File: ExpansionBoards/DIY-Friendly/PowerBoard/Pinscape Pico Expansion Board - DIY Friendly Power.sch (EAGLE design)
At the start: 83 parts, among them IC1 UCC27524P, IC10 ULN2803A, IC11 ULN2803A, IC12 ULN2803A, IC13 DS1307+, IC2 UCC27524P, IC3 UCC27524P, IC4 UCC27524P, IC5 UCC27524P, IC6 UCC27524P, IC7 UCC27524P, IC8 UCC27524P, IC9 ULN2803A, J1 640445-9, J2 640445-9, J3 640445-6, J4 1-640456-0, J5 1-640456-0, J6 1-640456-0, J7 1-640456-0, Q1 STP19NF20, Q10 STP19NF20, Q11 STP19NF20, Q12 STP19NF20, Q13 STP19NF20, Q14 STP19NF20, Q15 STP19NF20, Q16 STP19NF20, Q17 2N2222A, Q18 2N2222A, Q2 STP19NF20, Q3 STP19NF20, Q4 STP19NF20, Q5 STP19NF20, Q6 STP19NF20, Q7 STP19NF20, Q8 STP19NF20, Q9 STP19NF20, Y1 ECS-.327-12.5-13X-C

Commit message: Exp boards: update gate resistors in BOMs
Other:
- note added: "Note: Gate resistor value of 200 Ohms is chosen to protect UCC27524P against damage due to excessive power dissipation during PWM switching. In principle, the gate resistor is primarily to suppress ringing, which only requires a small resistor in the 5 to 10 Ohm range. But practical testing suggests that UCC27524P may be vulnerable to overload when used with MOSFETs with high input capacitance (C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"
- note removed: "Note: Gate resistor value of 200 Ohms is chosen to protect UCC27524P against damage due to excessive power dissipation during PWM switching. In principle, the gate resistor is primarily to suppress ringing, which only requires a small resistor in the 5 to 10 Ohm range. But practical testing shows that UCC27524P is vulnerable to overload when used with MOSFETs with high input capacitance (C[ISS]).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"
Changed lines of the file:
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@@
 In principle, the gate resistor is primarily to suppress
 ringing, which only requires a small resistor in the 5
-to 10 Ohm range.  But practical testing shows that
-UCC27524P is vulnerable to overload when used
+to 10 Ohm range.  But practical testing suggests that
+UCC27524P may be vulnerable to overload when used
 with MOSFETs with high input capacitance (C[ISS]).
 200 Ohms appears safe for common FETs such as

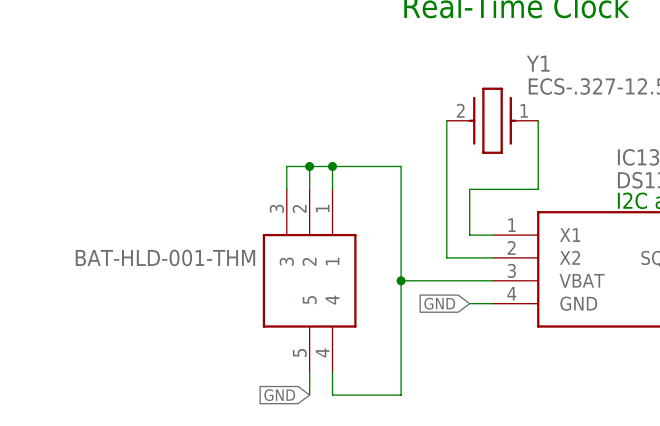
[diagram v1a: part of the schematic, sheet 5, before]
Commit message: exp board: DIY power: change battery holder to snap-in type
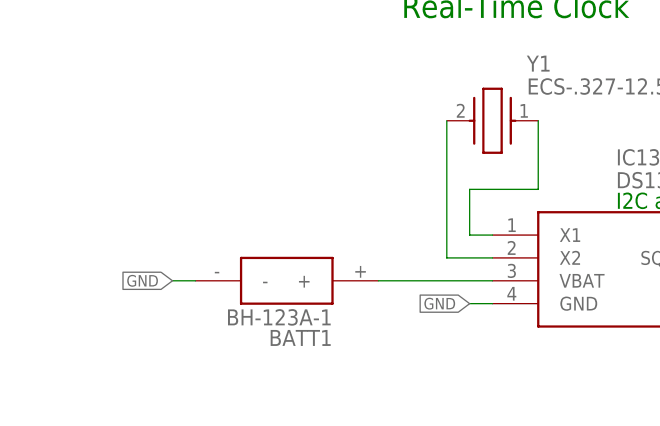
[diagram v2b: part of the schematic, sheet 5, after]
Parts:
- BATT1: value BAT-HLD-001-THM -> BH-123A-1; device SamacSys_Parts:BAT-HLD-001-THM -> SamacSys_Parts:BH-123A-1
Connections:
- net GND: now also BATT1.-; no longer BATT1.5
- net N$35: now also BATT1.+; no longer BATT1.1, BATT1.2, BATT1.3, BATT1.4
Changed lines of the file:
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@@
 <part name="IC12" library="uln-udn" deviceset="ULN2803A" device="" value="ULN2803A"/>
 <part name="J7" library="SamacSys_Parts" deviceset="1-640456-0" device=""/>
-<part name="BATT1" library="SamacSys_Parts" deviceset="BAT-HLD-001-THM" device=""/>
 <part name="IC13" library="SamacSys_Parts" deviceset="DS1307+" device=""/>
 <part name="Y1" library="SamacSys_Parts" deviceset="ECS-.327-12.5-13X-C" device=""/>
@@
 <part name="S1" library="switch-omron" deviceset="10-XX" device=""/>
 <part name="GND5" library="supply1" deviceset="GND" device=""/>
+<part name="BATT1" library="SamacSys_Parts" deviceset="BH-123A-1" device=""/>
 </parts>
 <sheets>
@@
 </plain>
 <instances>
-<instance part="BATT1" gate="G$1" x="40.64" y="30.48" smashed="yes" rot="R270">
-<attribute name="VALUE" x="32.258" y="22.86" size="1.778" layer="96" rot="R180" align="center-left"/>
-</instance>
 <instance part="IC13" gate="G$1" x="58.42" y="25.4" smashed="yes">
 <attribute name="NAME" x="72.136" y="34.036" size="1.778" layer="95" align="center-left"/>
@@
 </instance>
 <instance part="Y1" gate="G$1" x="53.34" y="38.1"/>
+<instance part="BATT1" gate="G$1" x="35.56" y="20.32" smashed="yes" rot="R180">
+<attribute name="NAME" x="40.64" y="13.97" size="1.778" layer="95" rot="R180" align="center-left"/>
+<attribute name="VALUE" x="40.64" y="16.256" size="1.778" layer="96" rot="R180" align="center-left"/>
+</instance>
 </instances>
 <busses>
@@
 <net name="GND" class="0">
 <segment>
-<pinref part="BATT1" gate="G$1" pin="5"/>
-<wire x1="38.1" y1="10.16" x2="38.1" y2="7.62" width="0.1524" layer="91"/>
-<label x="38.1" y="7.62" size="1.27" layer="95" rot="R180" xref="yes"/>
+<label x="22.86" y="20.32" size="1.27" layer="95" rot="R180" xref="yes"/>
+<wire x1="22.86" y1="20.32" x2="25.4" y2="20.32" width="0.1524" layer="91"/>
+<pinref part="BATT1" gate="G$1" pin="-"/>
 </segment>
 <segment>
@@
 <wire x1="58.42" y1="17.78" x2="55.88" y2="17.78" width="0.1524" layer="91"/>
 <label x="55.88" y="17.78" size="1.27" layer="95" rot="R180" xref="yes"/>
-</segment>
-</net>
-<net name="N$35" class="0">
-<segment>
-<pinref part="BATT1" gate="G$1" pin="3"/>
-<wire x1="35.56" y1="30.48" x2="35.56" y2="33.02" width="0.1524" layer="91"/>
-<wire x1="35.56" y1="33.02" x2="38.1" y2="33.02" width="0.1524" layer="91"/>
-<pinref part="BATT1" gate="G$1" pin="2"/>
-<wire x1="38.1" y1="33.02" x2="38.1" y2="30.48" width="0.1524" layer="91"/>
-<wire x1="38.1" y1="33.02" x2="40.64" y2="33.02" width="0.1524" layer="91"/>
-<junction x="38.1" y="33.02"/>
-<pinref part="BATT1" gate="G$1" pin="1"/>
-<wire x1="40.64" y1="33.02" x2="40.64" y2="30.48" width="0.1524" layer="91"/>
-<pinref part="BATT1" gate="G$1" pin="4"/>
-<wire x1="40.64" y1="10.16" x2="40.64" y2="7.62" width="0.1524" layer="91"/>
-<wire x1="40.64" y1="7.62" x2="48.26" y2="7.62" width="0.1524" layer="91"/>
-<wire x1="48.26" y1="7.62" x2="48.26" y2="20.32" width="0.1524" layer="91"/>
-<wire x1="48.26" y1="20.32" x2="48.26" y2="33.02" width="0.1524" layer="91"/>
-<wire x1="48.26" y1="33.02" x2="40.64" y2="33.02" width="0.1524" layer="91"/>
-<junction x="40.64" y="33.02"/>
-<pinref part="IC13" gate="G$1" pin="VBAT"/>
-<wire x1="58.42" y1="20.32" x2="48.26" y2="20.32" width="0.1524" layer="91"/>
-<junction x="48.26" y="20.32"/>
 </segment>
 </net>
@@
 </segment>
 </net>
+<net name="N$35" class="0">
+<segment>
+<pinref part="IC13" gate="G$1" pin="VBAT"/>
+<pinref part="BATT1" gate="G$1" pin="+"/>
+<wire x1="58.42" y1="20.32" x2="45.72" y2="20.32" width="0.1524" layer="91"/>
+</segment>
+</net>

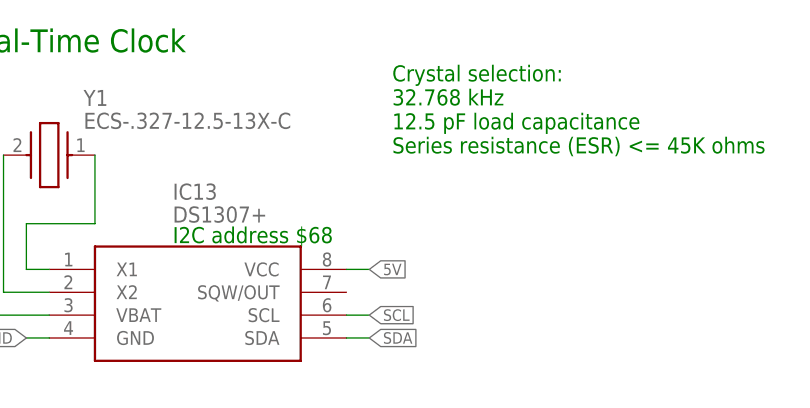
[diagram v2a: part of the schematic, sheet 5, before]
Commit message: exp board: power: change RTC power source to main Pico bus power
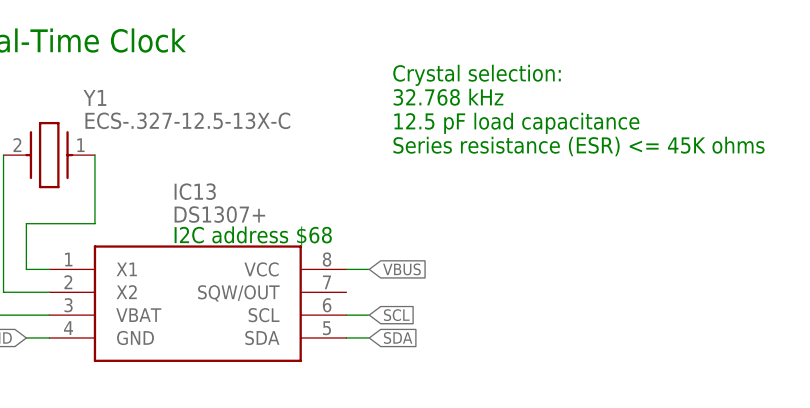
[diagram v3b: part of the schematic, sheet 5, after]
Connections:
- net 5V: no longer IC13.VCC
- net VBUS: now also IC13.VCC
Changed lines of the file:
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@@
-</segment>
-</net>
-<net name="5V" class="0">
-<segment>
-<pinref part="IC13" gate="G$1" pin="VCC"/>
-<wire x1="91.44" y1="25.4" x2="93.98" y2="25.4" width="0.1524" layer="91"/>
-<label x="93.98" y="25.4" size="1.27" layer="95" xref="yes"/>
 </segment>
 </net>
@@
 </segment>
 </net>
+<net name="VBUS" class="0">
+<segment>
+<pinref part="IC13" gate="G$1" pin="VCC"/>
+<wire x1="91.44" y1="25.4" x2="93.98" y2="25.4" width="0.1524" layer="91"/>
+<label x="93.98" y="25.4" size="1.27" layer="95" xref="yes"/>
+</segment>
+</net>

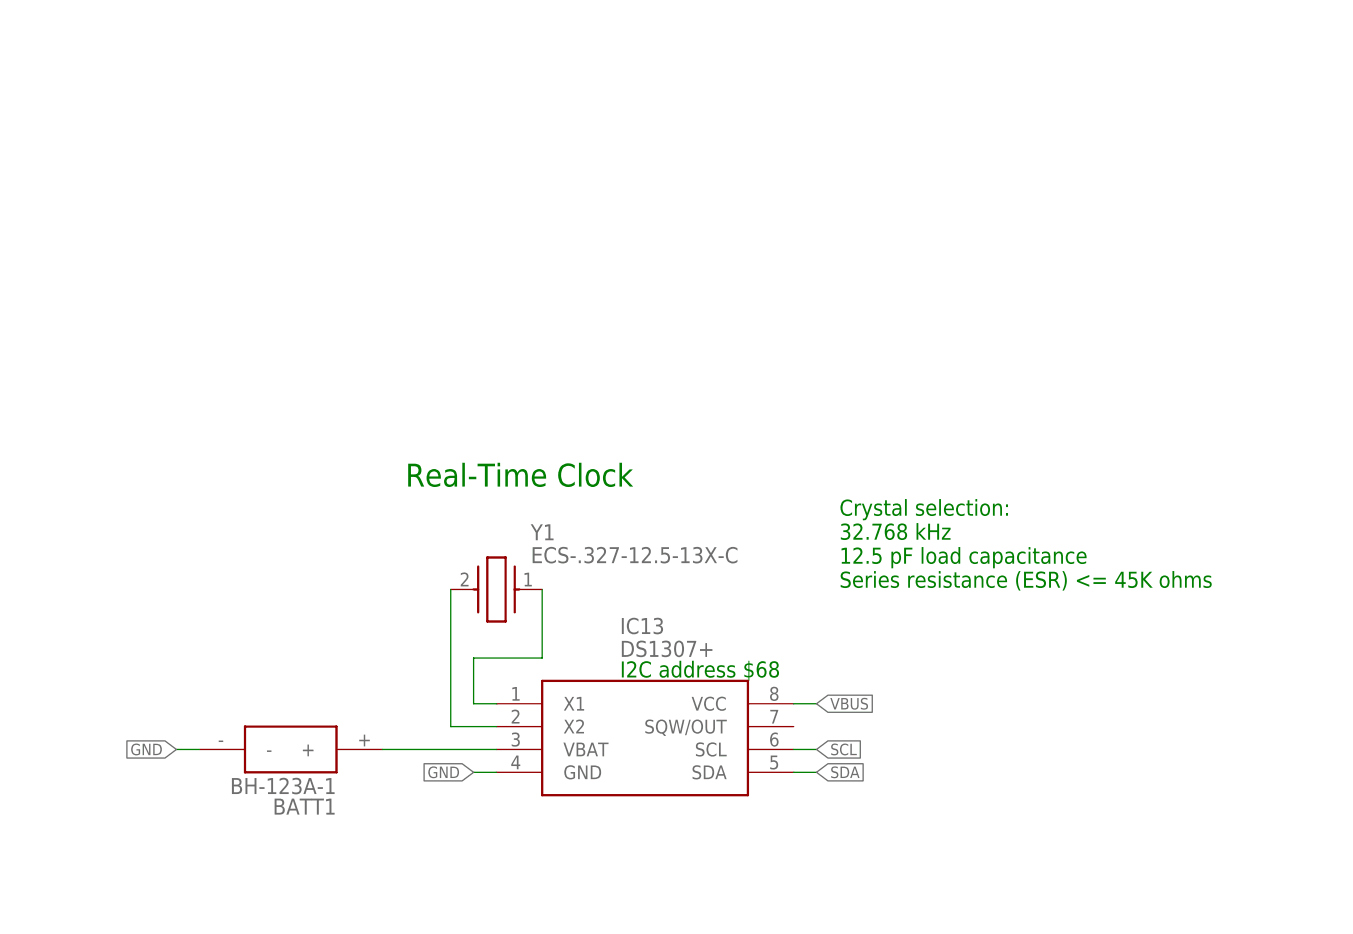
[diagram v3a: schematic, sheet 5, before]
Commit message: exp board: DIY power: add guard ring and isolated ground plane under DS1307 crystal per App Note 58
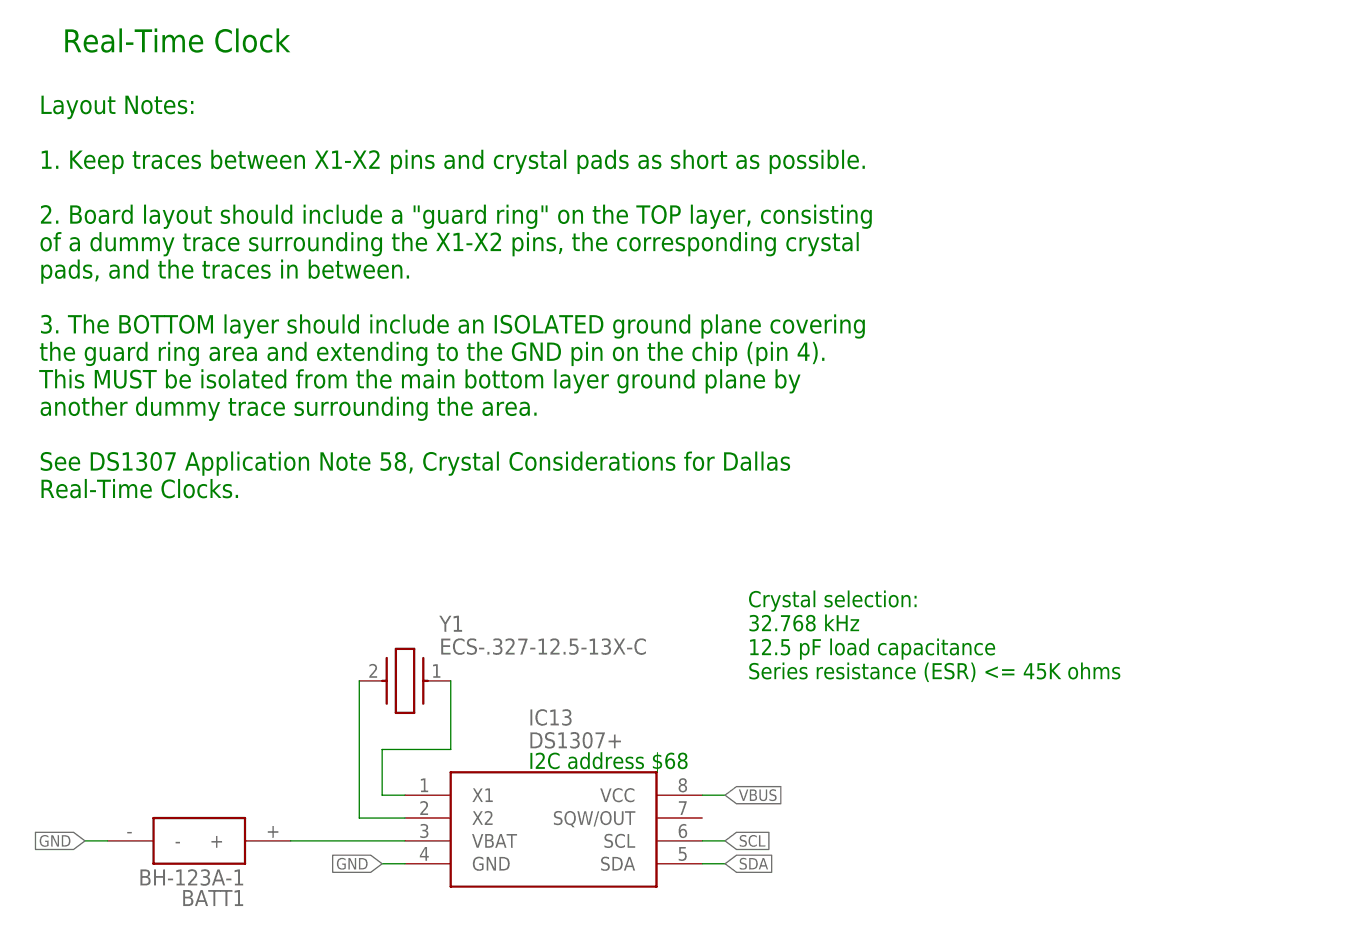
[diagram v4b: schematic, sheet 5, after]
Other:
- note added: "Layout Notes: 1. Keep traces between X1-X2 pins and crystal pads as short as possible. 2. Board layout should include a "guard ring" on the TOP layer, consisting of a dummy trace surrounding the X1-X2 pins, the corresponding crystal pads, and the traces in between. 3. The BOTTOM layer should include an ISOLATED ground plane covering the guard ring area and extending to the GND pin on the chip (pi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"
- moved on the sheet: BATT1, IC13, Y1
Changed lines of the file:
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@@
 <description>Real-Time Clock</description>
 <plain>
-<text x="60.96" y="50.8" size="2.54" layer="91" align="center">Real-Time Clock</text>
-<text x="96.52" y="43.18" size="1.778" layer="91" align="center-left">Crystal selection:
+<text x="22.86" y="99.06" size="2.54" layer="91" align="center">Real-Time Clock</text>
+<text x="86.36" y="33.02" size="1.778" layer="91" align="center-left">Crystal selection:
 32.768 kHz
 12.5 pF load capacitance
 Series resistance (ESR) &lt;= 45K ohms</text>
-<text x="72.136" y="29.21" size="1.778" layer="91" align="center-left">I2C address $68</text>
+<text x="61.976" y="19.05" size="1.778" layer="91" align="center-left">I2C address $68</text>
+<text x="7.62" y="48.26" size="2.032" layer="91">Layout Notes:
+1. Keep traces between X1-X2 pins and crystal pads as short as possible.
+2. Board layout should include a "guard ring" on the TOP layer, consisting
+of a dummy trace surrounding the X1-X2 pins, the corresponding crystal
+pads, and the traces in between.
+3. The BOTTOM layer should include an ISOLATED ground plane covering
+the guard ring area and extending to the GND pin on the chip (pin 4).
+This MUST be isolated from the main bottom layer ground plane by
+another dummy trace surrounding the area.
+See DS1307 Application Note 58, Crystal Considerations for Dallas
+Real-Time Clocks.</text>
 </plain>
 <instances>
-<instance part="IC13" gate="G$1" x="58.42" y="25.4" smashed="yes">
-<attribute name="NAME" x="72.136" y="34.036" size="1.778" layer="95" align="center-left"/>
-<attribute name="VALUE" x="72.136" y="31.496" size="1.778" layer="96" align="center-left"/>
+<instance part="IC13" gate="G$1" x="48.26" y="15.24" smashed="yes">
+<attribute name="NAME" x="61.976" y="23.876" size="1.778" layer="95" align="center-left"/>
+<attribute name="VALUE" x="61.976" y="21.336" size="1.778" layer="96" align="center-left"/>
 </instance>
-<instance part="Y1" gate="G$1" x="53.34" y="38.1"/>
-<instance part="BATT1" gate="G$1" x="35.56" y="20.32" smashed="yes" rot="R180">
-<attribute name="NAME" x="40.64" y="13.97" size="1.778" layer="95" rot="R180" align="center-left"/>
-<attribute name="VALUE" x="40.64" y="16.256" size="1.778" layer="96" rot="R180" align="center-left"/>
+<instance part="Y1" gate="G$1" x="43.18" y="27.94"/>
+<instance part="BATT1" gate="G$1" x="25.4" y="10.16" smashed="yes" rot="R180">
+<attribute name="NAME" x="30.48" y="3.81" size="1.778" layer="95" rot="R180" align="center-left"/>
+<attribute name="VALUE" x="30.48" y="6.096" size="1.778" layer="96" rot="R180" align="center-left"/>
 </instance>
 </instances>
@@
 <net name="GND" class="0">
 <segment>
-<label x="22.86" y="20.32" size="1.27" layer="95" rot="R180" xref="yes"/>
-<wire x1="22.86" y1="20.32" x2="25.4" y2="20.32" width="0.1524" layer="91"/>
+<label x="12.7" y="10.16" size="1.27" layer="95" rot="R180" xref="yes"/>
+<wire x1="12.7" y1="10.16" x2="15.24" y2="10.16" width="0.1524" layer="91"/>
 <pinref part="BATT1" gate="G$1" pin="-"/>
 </segment>
 <segment>
 <pinref part="IC13" gate="G$1" pin="GND"/>
-<wire x1="58.42" y1="17.78" x2="55.88" y2="17.78" width="0.1524" layer="91"/>
-<label x="55.88" y="17.78" size="1.27" layer="95" rot="R180" xref="yes"/>
+<wire x1="48.26" y1="7.62" x2="45.72" y2="7.62" width="0.1524" layer="91"/>
+<label x="45.72" y="7.62" size="1.27" layer="95" rot="R180" xref="yes"/>
 </segment>
 </net>
@@
 <segment>
 <pinref part="IC13" gate="G$1" pin="SCL"/>
-<wire x1="91.44" y1="20.32" x2="93.98" y2="20.32" width="0.1524" layer="91"/>
-<label x="93.98" y="20.32" size="1.27" layer="95" xref="yes"/>
+<wire x1="81.28" y1="10.16" x2="83.82" y2="10.16" width="0.1524" layer="91"/>
+<label x="83.82" y="10.16" size="1.27" layer="95" xref="yes"/>
 </segment>
 </net>
@@
 <segment>
 <pinref part="IC13" gate="G$1" pin="SDA"/>
-<wire x1="91.44" y1="17.78" x2="93.98" y2="17.78" width="0.1524" layer="91"/>
-<label x="93.98" y="17.78" size="1.27" layer="95" xref="yes"/>
+<wire x1="81.28" y1="7.62" x2="83.82" y2="7.62" width="0.1524" layer="91"/>
+<label x="83.82" y="7.62" size="1.27" layer="95" xref="yes"/>
 </segment>
 </net>
@@
 <segment>
 <pinref part="IC13" gate="G$1" pin="X1"/>
-<wire x1="58.42" y1="25.4" x2="55.88" y2="25.4" width="0.1524" layer="91"/>
-<wire x1="55.88" y1="25.4" x2="55.88" y2="30.48" width="0.1524" layer="91"/>
-<wire x1="55.88" y1="30.48" x2="63.5" y2="30.48" width="0.1524" layer="91"/>
+<wire x1="48.26" y1="15.24" x2="45.72" y2="15.24" width="0.1524" layer="91"/>
+<wire x1="45.72" y1="15.24" x2="45.72" y2="20.32" width="0.1524" layer="91"/>
+<wire x1="45.72" y1="20.32" x2="53.34" y2="20.32" width="0.1524" layer="91"/>
 <pinref part="Y1" gate="G$1" pin="CRYSTAL_1"/>
-<wire x1="63.5" y1="30.48" x2="63.5" y2="38.1" width="0.1524" layer="91"/>
+<wire x1="53.34" y1="20.32" x2="53.34" y2="27.94" width="0.1524" layer="91"/>
 </segment>
 </net>
@@
 <segment>
 <pinref part="Y1" gate="G$1" pin="CRYSTAL_2"/>
-<wire x1="53.34" y1="38.1" x2="53.34" y2="22.86" width="0.1524" layer="91"/>
+<wire x1="43.18" y1="27.94" x2="43.18" y2="12.7" width="0.1524" layer="91"/>
 <pinref part="IC13" gate="G$1" pin="X2"/>
-<wire x1="53.34" y1="22.86" x2="58.42" y2="22.86" width="0.1524" layer="91"/>
+<wire x1="43.18" y1="12.7" x2="48.26" y2="12.7" width="0.1524" layer="91"/>
 </segment>
 </net>
@@
 <pinref part="IC13" gate="G$1" pin="VBAT"/>
 <pinref part="BATT1" gate="G$1" pin="+"/>
-<wire x1="58.42" y1="20.32" x2="45.72" y2="20.32" width="0.1524" layer="91"/>
+<wire x1="48.26" y1="10.16" x2="35.56" y2="10.16" width="0.1524" layer="91"/>
 </segment>
 </net>
@@
 <segment>
 <pinref part="IC13" gate="G$1" pin="VCC"/>
-<wire x1="91.44" y1="25.4" x2="93.98" y2="25.4" width="0.1524" layer="91"/>
-<label x="93.98" y="25.4" size="1.27" layer="95" xref="yes"/>
+<wire x1="81.28" y1="15.24" x2="83.82" y2="15.24" width="0.1524" layer="91"/>
+<label x="83.82" y="15.24" size="1.27" layer="95" xref="yes"/>
 </segment>
 </net>
